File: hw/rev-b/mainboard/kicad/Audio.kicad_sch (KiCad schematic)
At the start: 27 parts, among them J21 AUDIO, Q4 SS8050, Q5 SS8050, Q6 SS8050, Q7 SS8550

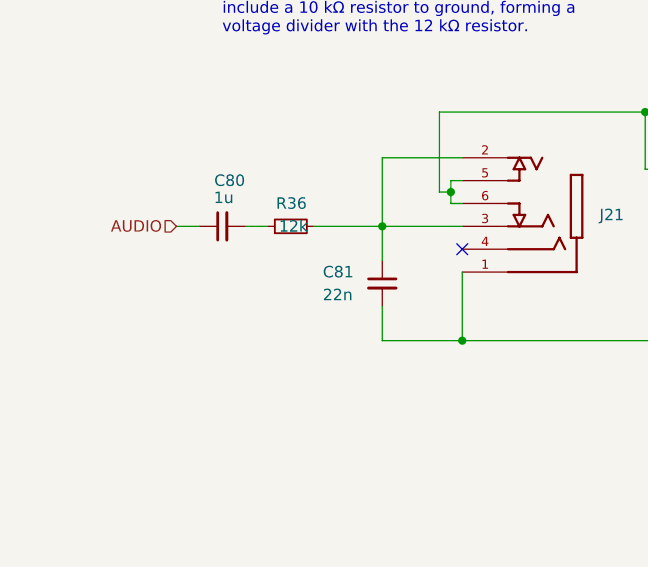
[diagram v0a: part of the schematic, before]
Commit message: hw: audio_det, stitching around sram
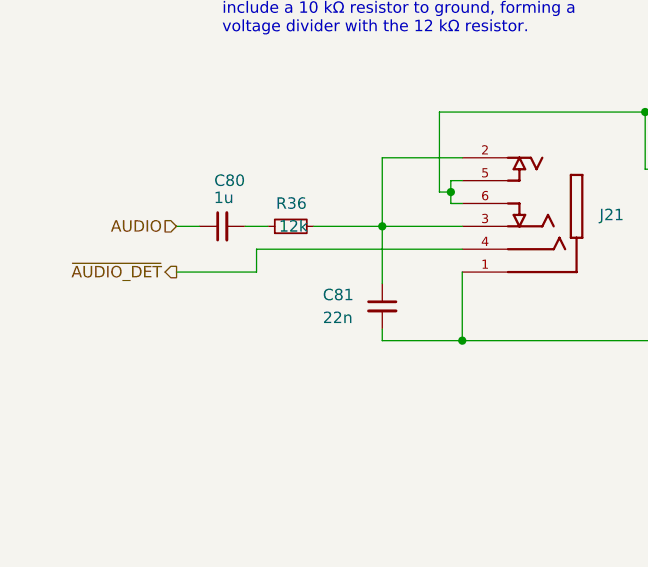
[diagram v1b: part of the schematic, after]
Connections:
- net ~{AUDIO_DET}: now reaches J21.4
- no-connect marks 1 -> 0
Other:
- moved on the sheet: C81
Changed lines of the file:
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@@
 		(color 0 0 0 0)
 	)
-	(no_connect
-		(at 73.66 109.22)
-	)
 	(wire
 		(pts
@@
 	(wire
 		(pts
+			(xy 41.91 111.76) (xy 50.8 111.76)
+		)
+		(stroke
+			(width 0)
+			(type default)
+		)
+	)
+	(wire
+		(pts
+			(xy 50.8 109.22) (xy 50.8 111.76)
+		)
+		(stroke
+			(width 0)
+			(type default)
+		)
+	)
+	(wire
+		(pts
 			(xy 93.98 100.33) (xy 100.33 100.33)
 		)
@@
 	(wire
 		(pts
-			(xy 64.77 115.57) (xy 64.77 119.38)
+			(xy 64.77 118.11) (xy 64.77 119.38)
 		)
 		(stroke
@@
 	(wire
 		(pts
-			(xy 64.77 106.68) (xy 64.77 110.49)
+			(xy 64.77 106.68) (xy 64.77 113.03)
 		)
 		(stroke
@@
 		(pts
 			(xy 107.95 86.36) (xy 107.95 85.09)
+		)
+		(stroke
+			(width 0)
+			(type default)
+		)
+	)
+	(wire
+		(pts
+			(xy 73.66 109.22) (xy 50.8 109.22)
 		)
 		(stroke
@@
 			)
 			(justify left)
+		)
+	)
+	(hierarchical_label "~{AUDIO_DET}"
+		(shape output)
+		(at 41.91 111.76 180)
+		(fields_autoplaced yes)
+		(effects
+			(font
+				(size 1.27 1.27)
+			)
+			(justify right)
 		)
 	)
@@
 	(symbol
 		(lib_id "Device:C_Small")
-		(at 64.77 113.03 0)
+		(at 64.77 115.57 0)
 		(unit 1)
 		(exclude_from_sim no)
@@
 		(dnp no)
 		(property "Reference" "C81"
-			(at 58.166 111.76 0)
+			(at 58.166 114.3 0)
 			(effects
 				(font
@@
 		)
 		(property "Value" "22n"
-			(at 58.166 114.3 0)
+			(at 58.166 116.84 0)
 			(effects
 				(font
@@
 		)
 		(property "Footprint" "Capacitor_SMD:C_0402_1005Metric"
-			(at 64.77 113.03 0)
+			(at 64.77 115.57 0)
 			(effects
 				(font
@@
 		)
 		(property "Datasheet" "https://www.lcsc.com/datasheet/lcsc_datasheet_2304140030_FH--Guangdong-Fenghua-Advanced-Tech-0402B223K500NT_C1532.pdf"
-			(at 64.77 113.03 0)
+			(at 64.77 115.57 0)
 			(effects
 				(font
@@
 		)
 		(property "Description" ""
-			(at 64.77 113.03 0)
+			(at 64.77 115.57 0)
 			(effects
 				(font
@@
 		)
 		(property "LCSC" "C1532"
-			(at 64.77 113.03 0)
-			(effects
-				(font
+			(at 64.77 115.57 0)
+			(effects
+				(font
